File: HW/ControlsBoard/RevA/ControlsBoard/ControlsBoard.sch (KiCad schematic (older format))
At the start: 0 parts

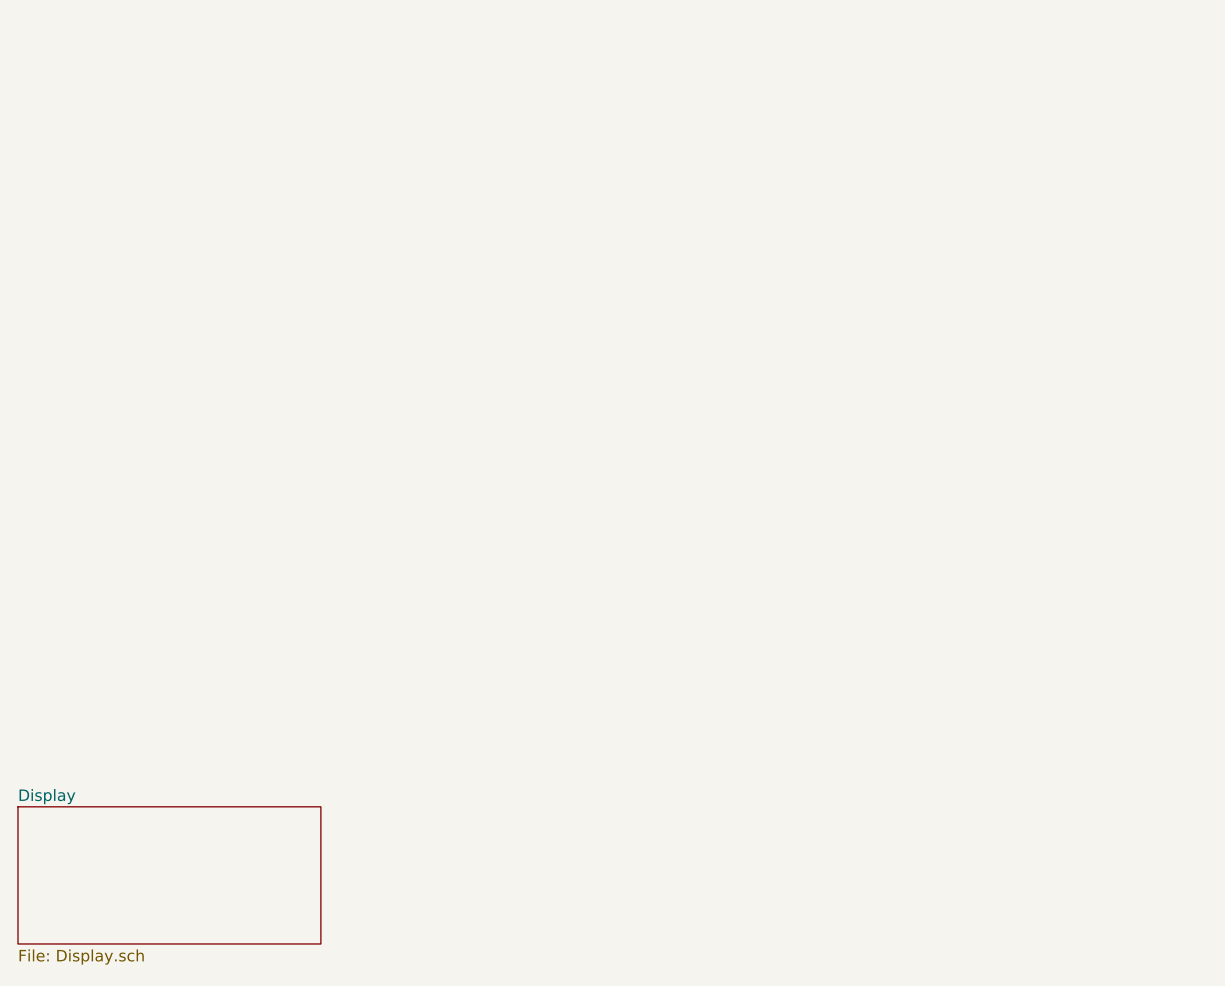
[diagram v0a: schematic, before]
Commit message: updated front panel board layouts
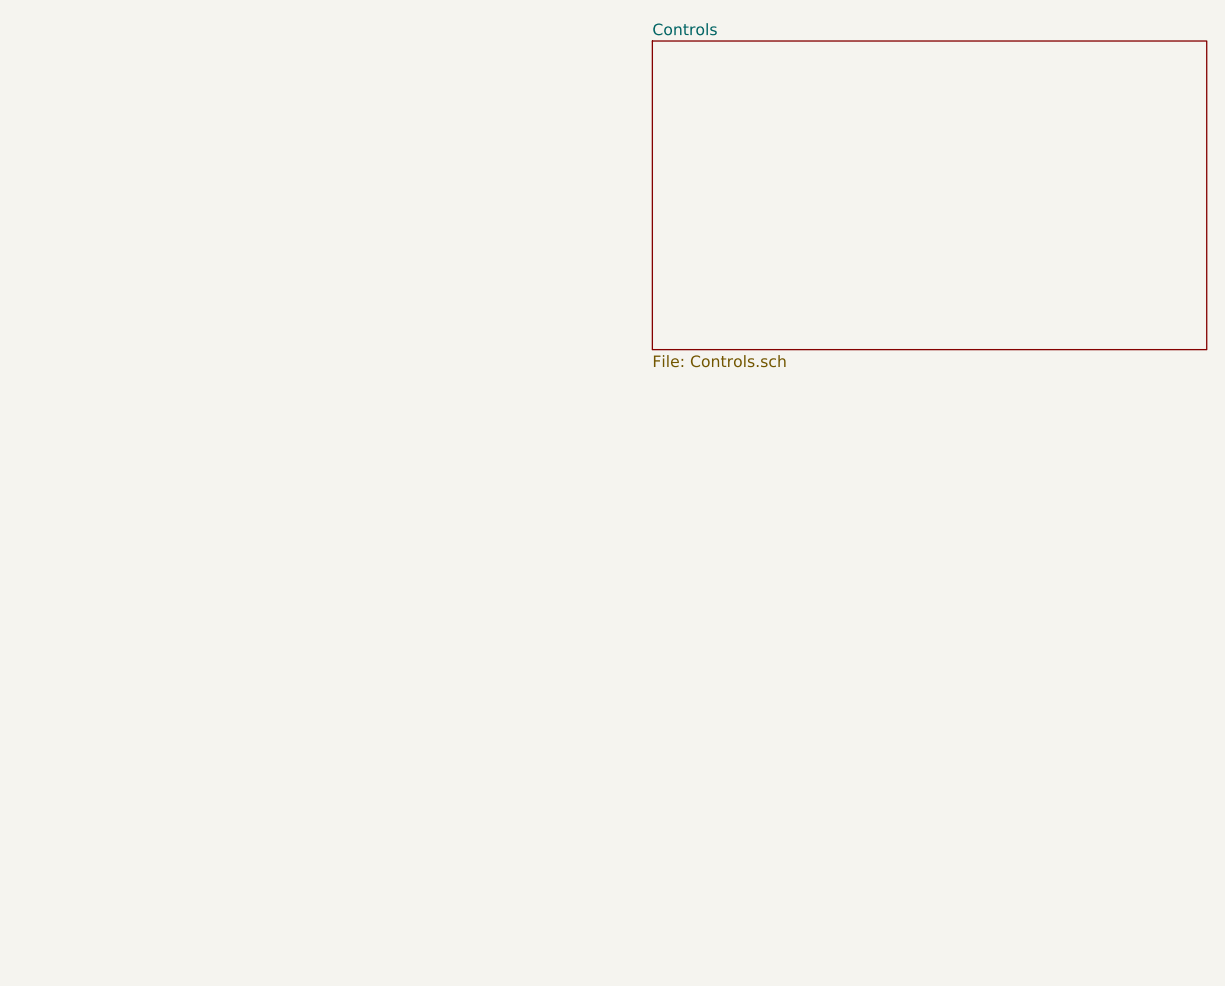
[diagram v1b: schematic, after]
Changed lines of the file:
@@
 encoding utf-8
 Sheet 1 2
-Title "Control Front Panel for Rotary Encoder and Tactile SPST"
-Date "2020-03-13"
-Rev "A"
+Title ""
+Date ""
+Rev ""
 Comp ""
 Comment1 ""
@@
 $EndDescr
 $Sheet
-S 1400 5500 1325 600
-U 5E7D4116
-F0 "Display" 50
-F1 "Display.sch" 50
+S 4175 2150 2425 1350
+U 5E7E6C1D
+F0 "Controls" 50
+F1 "Controls.sch" 50
 $EndSheet
 $EndSCHEMATC
